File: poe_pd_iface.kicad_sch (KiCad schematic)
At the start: 11 parts, among them U2 NCP1090, U3 PG02S4803A

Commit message: add pg02s 3D model
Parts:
- U3: footprint AlexComponents:PG02S -> newam:PG02S; digikey (none) -> 941-1186-ND
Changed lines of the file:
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@@
       (effects (font (size 1.524 1.524)))
     )
-    (property "Footprint" "AlexComponents:PG02S" (id 2) (at 173.99 124.46 0)
+    (property "Footprint" "newam:PG02S" (id 2) (at 173.99 124.46 0)
       (effects (font (size 1.524 1.524)) (justify left) hide)
     )
@@
       (effects (font (size 1.524 1.524)) (justify left) hide)
     )
+    (property "digikey" "941-1186-ND" (id 5) (at 176.53 113.03 0)
+      (effects (font (size 1.524 1.524)) (justify left) hide)
+    )

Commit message: NCP1090: NCP1090DGOS-ND -> NCP1090DRGOSCT-ND
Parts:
- U2: DigiKey Part Number NCP1090DGOS-ND -> NCP1090DRGOSCT-ND
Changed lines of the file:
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@@
       (effects (font (size 1.524 1.524)) hide)
     )
-    (property "DigiKey Part Number" "NCP1090DGOS-ND" (id 4) (at 143.51 116.84 0)
+    (property "DigiKey Part Number" "NCP1090DRGOSCT-ND" (id 4) (at 143.51 116.84 0)
       (effects (font (size 1.524 1.524)) hide)
     )

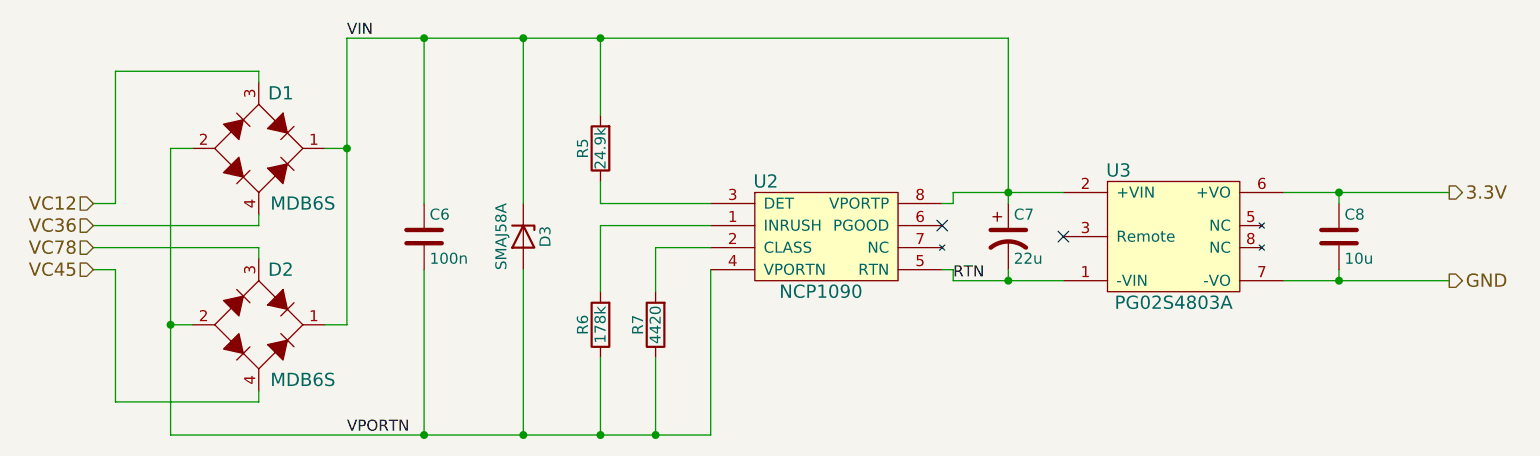
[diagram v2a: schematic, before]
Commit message: 22uF electrolytic: replace with 27uF for stock reasons
399-A768KE226M1JLAE054TR-ND -> 399-A768KE276M1JLAE054CT-ND
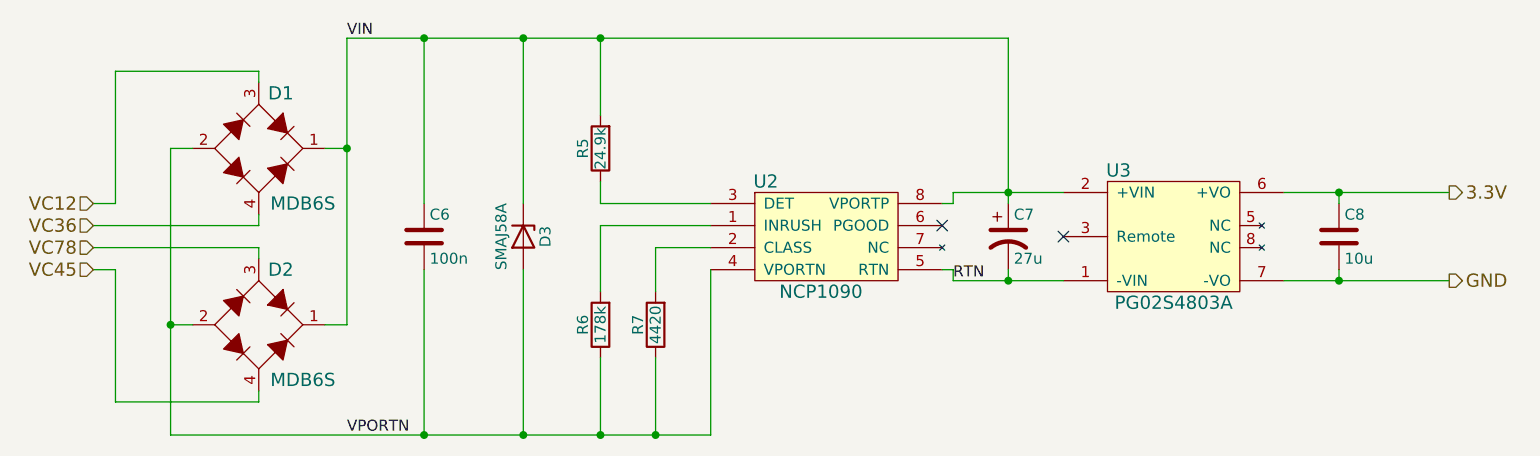
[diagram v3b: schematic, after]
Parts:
- C7: value 22u -> 27u; DigiKey Part Number 399-A768KE226M1JLAE054TR-ND -> 399-A768KE276M1JLAE054CT-ND
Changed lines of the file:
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@@
       (effects (font (size 1.27 1.27)) (justify left))
     )
-    (property "Value" "22u" (id 1) (at 165.735 105.41 0)
+    (property "Value" "27u" (id 1) (at 165.735 105.41 0)
       (effects (font (size 1.27 1.27)) (justify left))
     )
@@
       (effects (font (size 1.27 1.27)) hide)
     )
-    (property "DigiKey Part Number" "399-A768KE226M1JLAE054TR-ND" (id 4) (at 165.1 102.87 0)
+    (property "DigiKey Part Number" "399-A768KE276M1JLAE054CT-ND" (id 4) (at 165.1 102.87 0)
       (effects (font (size 1.524 1.524)) hide)
     )

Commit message: add mounting holes, replace magjack with in-stock part
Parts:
- U3: DigiKey Part Number 941-1186-ND -> 941-1185-ND
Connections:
- net VC12: now also D2.3 (AC1); no longer D1.3 (AC1)
- net VC36: now also D2.4 (AC2); no longer D1.4 (AC2)
- net VC45: now also D1.3 (AC1); no longer D2.4 (AC2)
- net VC78: now also D1.4 (AC2); no longer D2.3 (AC1)
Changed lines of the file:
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@@
     (effects (font (size 1.27 1.27)) (justify left bottom))
   )
-  (hierarchical_label "VC12" (shape input) (at 59.69 99.06 180)
+  (hierarchical_label "VC12" (shape input) (at 59.69 104.14 180)
     (effects (font (size 1.524 1.524)) (justify right))
   )
@@
     (effects (font (size 1.524 1.524)) (justify left))
   )
-  (hierarchical_label "VC36" (shape input) (at 59.69 101.6 180)
+  (hierarchical_label "VC36" (shape input) (at 59.69 106.68 180)
     (effects (font (size 1.524 1.524)) (justify right))
   )
@@
     (effects (font (size 1.524 1.524)) (justify left))
   )
-  (hierarchical_label "VC78" (shape input) (at 59.69 104.14 180)
-    (effects (font (size 1.524 1.524)) (justify right))
-  )
-  (hierarchical_label "VC45" (shape input) (at 59.69 106.68 180)
+  (hierarchical_label "VC78" (shape input) (at 59.69 101.6 180)
+    (effects (font (size 1.524 1.524)) (justify right))
+  )
+  (hierarchical_label "VC45" (shape input) (at 59.69 99.06 180)
     (effects (font (size 1.524 1.524)) (justify right))
   )
@@
       (effects (font (size 1.524 1.524)) (justify left) hide)
     )
-    (property "DigiKey Part Number" "941-1186-ND" (id 4) (at 176.53 113.03 0)
-      (effects (font (size 1.524 1.524)) (justify left) hide)
-    )
+    (property "DigiKey Part Number" "941-1185-ND" (id 4) (at 176.53 113.03 0)
+      (effects (font (size 1.524 1.524)) (justify left) hide)
+    )
